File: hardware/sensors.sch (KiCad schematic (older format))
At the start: 16 parts

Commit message: Almost finished layout
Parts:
- removed L?: 330u, symbol L_Small
- C30, C31, C33: renamed from C?; footprint (none) -> Capacitors_SMD:C_1210
- C32: renamed from C?; value 47u -> 10u; footprint (none) -> Capacitors_ThroughHole:C_Radial_D5_L11_P2
- L3: renamed from L?; value Wurth 74275043 -> Wurth WE-CBF; footprint (none) -> Choke_SMD:Choke_SMD_1206_Standard
- P6: renamed from P?; value NORPS-12 -> NSL-19M51; footprint Luna_Optoelectronics_LDR:NORPS-12 -> TO_SOT_Packages_THT:TO-18_2Pin
- P7: renamed from P?; footprint Terminal_Blocks:TerminalBlock_Pheonix_MKDS1.5-5pol -> Connectors_Molex:Molex_KK-6410-05_05x2.54mm_Straight
- R24, R25, R26, R27, R28, R29, R30: renamed from R?; footprint (none) -> Resistors_SMD:R_1210
- gave numbers to parts that had none: 1
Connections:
- net 5VA: now also C32.1, C33.2, P7.3 (P3)
- net 3V3D: now reaches C31.1, L3.2, R25.1, R26.1, U3.2 (CSB), U3.6 (V_DDIO)
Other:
- note removed: "1.2kHz low pass"
- moved on the sheet: L3
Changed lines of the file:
@@
 LIBS:valves
 LIBS:wiznet
-LIBS:Sensors_STMicroelectronics
 LIBS:Sensors_Bosch
 LIBS:environment-sensor-cache
@@
 Enclosure must be aluminium to avoid hurting magnetic field measurements (mu << 1)\n\nhttps://physics.stackexchange.com/questions/6524/which-metals-can-cause-magnetic-interference-passively
 $Comp
-L Bosch_BME280 U?
+L Bosch_BME280 U3
 U 1 1 5893AF35
 P 7250 2400
-F 0 "U?" H 7250 2950 50  0000 C CNN
+F 0 "U3" H 7250 2950 50  0000 C CNN
 F 1 "Bosch_BME280" H 7250 1850 50  0000 C CNN
 F 2 "Bosch_Environment_Sensor:Bosch_BME280_LGA-8" H 7250 2400 60  0001 C CNN
@@
 $EndComp
 $Comp
-L C_Small C?
+L C_Small C31
 U 1 1 58F4F4F4
 P 5700 2400
-F 0 "C?" H 5750 2450 50  0000 L CNN
+F 0 "C31" H 5750 2450 50  0000 L CNN
 F 1 "100n" H 5750 2350 50  0000 L CNN
-F 2 "" H 5700 2400 50  0000 C CNN
+F 2 "Capacitors_SMD:C_1210" H 5700 2400 50  0001 C CNN
 F 3 "" H 5700 2400 50  0000 C CNN
 	1    5700 2400
@@
 Address = 1110110 (0x76)
 $Comp
-L R_Small R?
+L R_Small R26
 U 1 1 58F5028C
 P 6300 2450
-F 0 "R?" H 6350 2500 50  0000 L CNN
+F 0 "R26" H 6350 2500 50  0000 L CNN
 F 1 "4k7" H 6350 2400 50  0000 L CNN
-F 2 "" H 6300 2450 50  0000 C CNN
+F 2 "Resistors_SMD:R_1210" H 6300 2450 50  0001 C CNN
 F 3 "" H 6300 2450 50  0000 C CNN
 	1    6300 2450
@@
 $EndComp
 $Comp
-L R_Small R?
+L R_Small R25
 U 1 1 58F50586
 P 6200 2450
-F 0 "R?" H 6050 2500 50  0000 L CNN
+F 0 "R25" H 6050 2500 50  0000 L CNN
 F 1 "4k7" H 6000 2400 50  0000 L CNN
-F 2 "" H 6200 2450 50  0000 C CNN
+F 2 "Resistors_SMD:R_1210" H 6200 2450 50  0001 C CNN
 F 3 "" H 6200 2450 50  0000 C CNN
 	1    6200 2450
@@
 3V3A
 $Comp
-L C_Small C?
+L C_Small C30
 U 1 1 58F50E9D
 P 5300 2400
-F 0 "C?" H 5150 2450 50  0000 L CNN
+F 0 "C30" H 5150 2450 50  0000 L CNN
 F 1 "100n" H 5050 2350 50  0000 L CNN
-F 2 "" H 5300 2400 50  0000 C CNN
+F 2 "Capacitors_SMD:C_1210" H 5300 2400 50  0001 C CNN
 F 3 "" H 5300 2400 50  0000 C CNN
 	1    5300 2400
@@
 $EndComp
 $Comp
-L L_Small L?
+L L_Small L3
 U 1 1 58F5F3B6
-P 5500 2000
-F 0 "L?" H 5530 2040 50  0000 L CNN
-F 1 "Wurth 74275043" H 5530 1960 50  0000 L CNN
-F 2 "" H 5500 2000 50  0000 C CNN
-F 3 "" H 5500 2000 50  0000 C CNN
-	1    5500 2000
+P 5500 1400
+F 0 "L3" H 5530 1440 50  0000 L CNN
+F 1 "Wurth WE-CBF" H 5530 1360 50  0000 L CNN
+F 2 "Choke_SMD:Choke_SMD_1206_Standard" H 5500 1400 50  0001 C CNN
+F 3 "" H 5500 1400 50  0000 C CNN
+	1    5500 1400
 	0    -1   -1   0
 $EndComp
 $Comp
-L CONN_01X05 P?
+L CONN_01X05 P7
 U 1 1 58F69CD9
 P 7700 4725
-F 0 "P?" H 7700 5025 50  0000 C CNN
+F 0 "P7" H 7700 5025 50  0000 C CNN
 F 1 "PPD42" V 7800 4725 50  0000 C CNN
-F 2 "Terminal_Blocks:TerminalBlock_Pheonix_MKDS1.5-5pol" H 7700 4725 50  0001 C CNN
+F 2 "Connectors_Molex:Molex_KK-6410-05_05x2.54mm_Straight" H 7700 4725 50  0001 C CNN
 F 3 "" H 7700 4725 50  0000 C CNN
 	1    7700 4725
@@
 5VA
 $Comp
-L C_Small C?
+L C_Small C33
 U 1 1 58F4E0C6
 P 6625 4550
-F 0 "C?" H 6635 4620 50  0000 L CNN
+F 0 "C33" H 6635 4620 50  0000 L CNN
 F 1 "100n" H 6635 4470 50  0000 L CNN
-F 2 "" H 6625 4550 50  0000 C CNN
+F 2 "Capacitors_SMD:C_1210" H 6625 4550 50  0001 C CNN
 F 3 "" H 6625 4550 50  0000 C CNN
 	1    6625 4550
@@
 $EndComp
 Wire Wire Line
-	6200 2000 6200 2300
-Wire Wire Line
-	6200 2300 6200 2350
-Wire Wire Line
-	6200 2300 6300 2300
-Wire Wire Line
-	6300 2300 6650 2300
+	6200 2000 6200 2350
+Wire Wire Line
+	6200 2300 6650 2300
 Wire Wire Line
 	7850 2400 7925 2400
@@
 	5700 2800 5700 2500
 Wire Wire Line
-	5200 2800 5300 2800
-Wire Wire Line
-	5300 2800 5700 2800
-Wire Wire Line
-	5700 2800 6600 2800
-Wire Wire Line
-	6600 2800 6650 2800
+	5200 2800 6650 2800
 Wire Wire Line
 	6650 2700 6600 2700
@@
 	6500 2400 6500 2600
 Wire Wire Line
-	6500 2600 6300 2600
-Wire Wire Line
-	6300 2600 6150 2600
+	6500 2600 6150 2600
 Wire Wire Line
 	6300 2600 6300 2550
@@
 	6550 2500 6550 2700
 Wire Wire Line
-	6550 2700 6200 2700
-Wire Wire Line
-	6200 2700 6150 2700
+	6550 2700 6150 2700
 Wire Wire Line
 	6200 2700 6200 2550
@@
 Connection ~ 6200 2700
 Wire Wire Line
-	5200 2100 5300 2100
-Wire Wire Line
-	5300 2100 6650 2100
+	5200 2100 6650 2100
 Wire Wire Line
 	5300 2800 5300 2500
 Connection ~ 5700 2800
-Wire Wire Line
-	5300 2000 5300 2100
-Wire Wire Line
-	5300 2100 5300 2300
 Connection ~ 5300 2100
 Wire Wire Line
-	5600 2000 5700 2000
-Wire Wire Line
-	5700 2000 6200 2000
-Wire Wire Line
-	6200 2000 6650 2000
-Wire Wire Line
-	5400 2000 5300 2000
+	5600 2000 6650 2000
 Connection ~ 5300 2800
 $Comp
-L CP_Small C?
+L CP_Small C32
 U 1 1 58F4E384
 P 6475 4550
-F 0 "C?" H 6485 4620 50  0000 L CNN
-F 1 "47u" H 6485 4470 50  0000 L CNN
-F 2 "" H 6475 4550 50  0000 C CNN
+F 0 "C32" H 6485 4620 50  0000 L CNN
+F 1 "10u" H 6485 4470 50  0000 L CNN
+F 2 "Capacitors_ThroughHole:C_Radial_D5_L11_P2" H 6475 4550 50  0001 C CNN
 F 3 "" H 6475 4550 50  0000 C CNN
 	1    6475 4550
@@
 $EndComp
 Wire Wire Line
-	6025 4375 6475 4375
-Wire Wire Line
-	6475 4375 6625 4375
-Wire Wire Line
-	6625 4375 7350 4375
+	6025 4375 7350 4375
 Wire Wire Line
 	6475 4375 6475 4450
@@
 Connection ~ 6625 4375
 Wire Wire Line
-	6300 4725 6475 4725
-Wire Wire Line
-	6475 4725 6625 4725
-Wire Wire Line
-	6625 4725 7500 4725
+	6025 4725 7500 4725
 Wire Wire Line
 	6475 4725 6475 4650
@@
 Tempertature/humidity/pressure sensor
 $Comp
-L R_Small R?
+L R_Small R29
 U 1 1 58F597C3
 P 6850 5100
-F 0 "R?" H 6700 5100 50  0000 L CNN
+F 0 "R29" H 6700 5100 50  0000 L CNN
 F 1 "10k" H 6675 5175 50  0000 L CNN
-F 2 "" H 6850 5100 50  0000 C CNN
+F 2 "Resistors_SMD:R_1210" H 6850 5100 50  0001 C CNN
 F 3 "" H 6850 5100 50  0000 C CNN
 	1    6850 5100
@@
 $EndComp
 $Comp
-L R_Small R?
+L R_Small R27
 U 1 1 58F5987E
 P 6675 5100
-F 0 "R?" H 6725 5100 50  0000 L CNN
+F 0 "R27" H 6725 5100 50  0000 L CNN
 F 1 "10k" H 6725 5175 50  0000 L CNN
-F 2 "" H 6675 5100 50  0000 C CNN
+F 2 "Resistors_SMD:R_1210" H 6675 5100 50  0001 C CNN
 F 3 "" H 6675 5100 50  0000 C CNN
 	1    6675 5100
@@
 $EndComp
 $Comp
-L R_Small R?
+L R_Small R30
 U 1 1 58F59C27
 P 6850 5400
-F 0 "R?" H 6700 5400 50  0000 L CNN
+F 0 "R30" H 6700 5400 50  0000 L CNN
 F 1 "10k" H 6675 5475 50  0000 L CNN
-F 2 "" H 6850 5400 50  0000 C CNN
+F 2 "Resistors_SMD:R_1210" H 6850 5400 50  0001 C CNN
 F 3 "" H 6850 5400 50  0000 C CNN
 	1    6850 5400
@@
 $EndComp
 $Comp
-L R_Small R?
+L R_Small R28
 U 1 1 58F59C75
 P 6675 5400
-F 0 "R?" H 6725 5400 50  0000 L CNN
+F 0 "R28" H 6725 5400 50  0000 L CNN
 F 1 "10k" H 6725 5475 50  0000 L CNN
-F 2 "" H 6675 5400 50  0000 C CNN
+F 2 "Resistors_SMD:R_1210" H 6675 5400 50  0001 C CNN
 F 3 "" H 6675 5400 50  0000 C CNN
 	1    6675 5400
@@
 	6600 5250 6675 5250
 Wire Wire Line
-	6675 5200 6675 5250
-Wire Wire Line
-	6675 5250 6675 5300
+	6675 5200 6675 5300
 Connection ~ 6675 5250
 Wire Wire Line
@@
 	6850 5000 6850 4625
 Wire Wire Line
-	6850 5200 6850 5250
-Wire Wire Line
-	6850 5250 6850 5300
+	6850 5200 6850 5300
 Wire Wire Line
 	6925 5250 6850 5250
@@
 GND
 Wire Wire Line
-	6600 5575 6675 5575
-Wire Wire Line
-	6675 5575 6850 5575
+	6600 5575 6850 5575
 Wire Wire Line
 	6675 5575 6675 5500
@@
 Connection ~ 6675 5575
 $Comp
-L L_Small L?
-U 1 1 58F5B341
-P 6200 4725
-F 0 "L?" H 6230 4765 50  0000 L CNN
-F 1 "330u" H 6230 4685 50  0000 L CNN
-F 2 "" H 6200 4725 50  0000 C CNN
-F 3 "" H 6200 4725 50  0000 C CNN
-	1    6200 4725
-	0    -1   -1   0
-$EndComp
-Wire Wire Line
-	6025 4725 6100 4725
-Text Notes 6075 4325 0    60   ~ 0
-1.2kHz low pass
-$Comp
-L CONN_01X02 P?
+L CONN_01X02 P6
 U 1 1 58F66D18
 P 4200 4475
-F 0 "P?" H 4200 4625 50  0000 C CNN
-F 1 "NORPS-12" V 4300 4475 50  0000 C CNN
-F 2 "Luna_Optoelectronics_LDR:NORPS-12" H 4200 4475 50  0001 C CNN
+F 0 "P6" H 4200 4625 50  0000 C CNN
+F 1 "NSL-19M51" V 4300 4475 50  0000 C CNN
+F 2 "TO_SOT_Packages_THT:TO-18_2Pin" H 4200 4475 50  0001 C CNN
 F 3 "" H 4200 4475 50  0000 C CNN
 	1    4200 4475
@@
 LDR_OUT
 Wire Wire Line
-	4000 4525 3825 4525
-Wire Wire Line
-	3825 4525 3750 4525
-$Comp
-L R_Small R?
+	3750 4525 4000 4525
+$Comp
+L R_Small R24
 U 1 1 58F672FB
 P 3825 4700
-F 0 "R?" H 3855 4720 50  0000 L CNN
+F 0 "R24" H 3855 4720 50  0000 L CNN
 F 1 "10k" H 3855 4660 50  0000 L CNN
-F 2 "" H 3825 4700 50  0000 C CNN
+F 2 "Resistors_SMD:R_1210" H 3825 4700 50  0001 C CNN
 F 3 "" H 3825 4700 50  0000 C CNN
 	1    3825 4700
@@
 Text Notes 3650 4200 0    60   ~ 0
 Light sensor
+Text Label 5775 1400 0    60   ~ 0
+3V3D
+Wire Wire Line
+	5775 1400 5600 1400
+Text HLabel 5200 1400 0    60   Input ~ 0
+3V3A
+Wire Wire Line
+	5200 1400 5400 1400
+Wire Wire Line
+	5300 2300 5300 2100
+Text Label 5600 2000 2    60   ~ 0
+3V3D
 $EndSCHEMATC

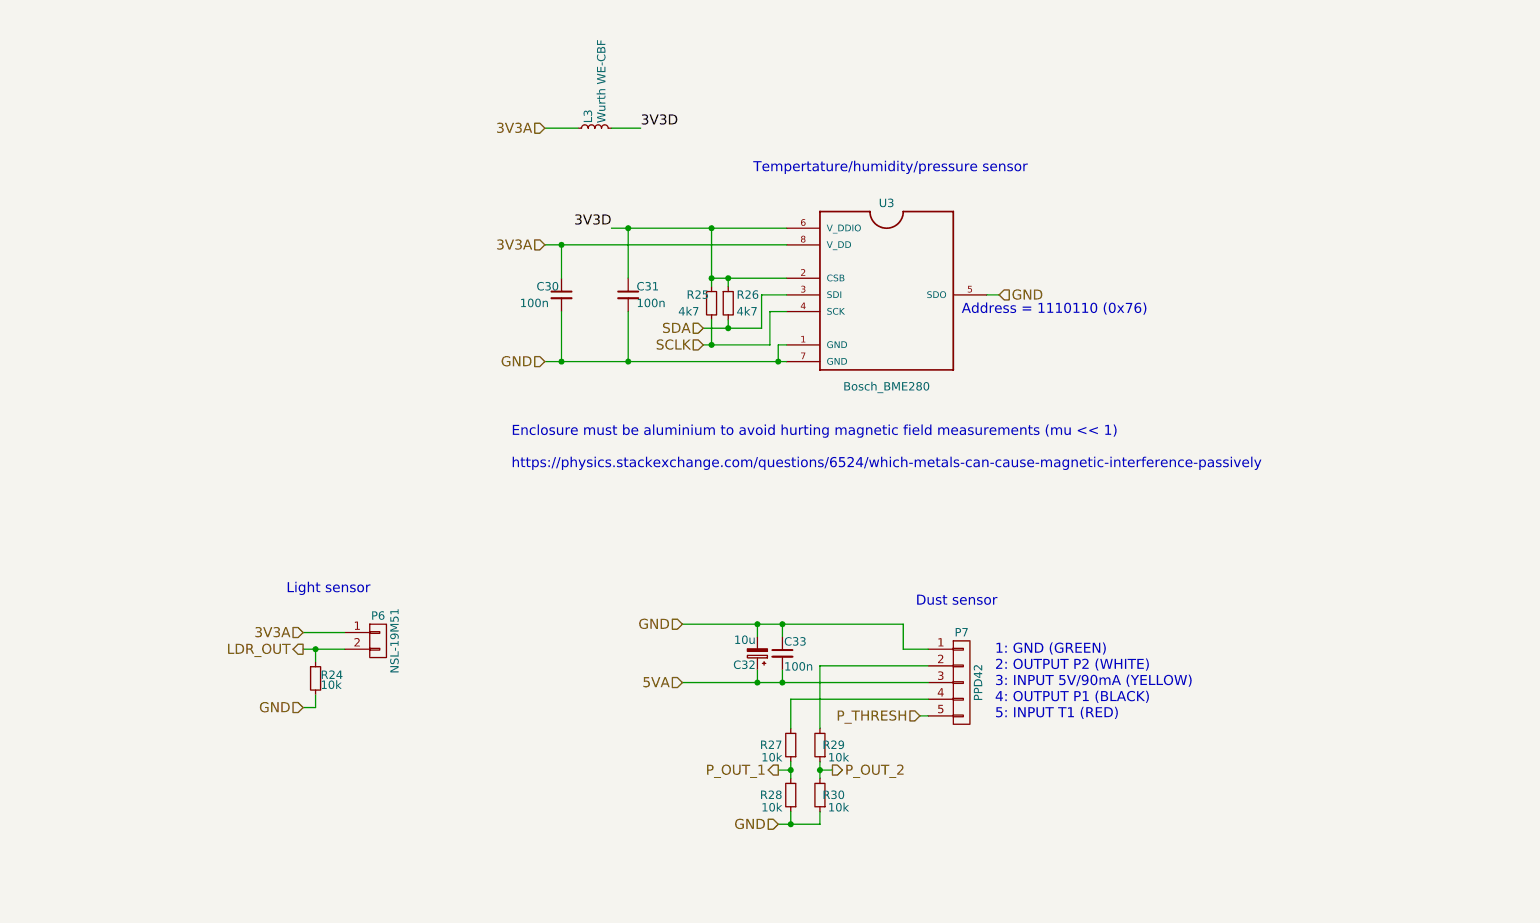
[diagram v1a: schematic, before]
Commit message: Revision of board to address issues
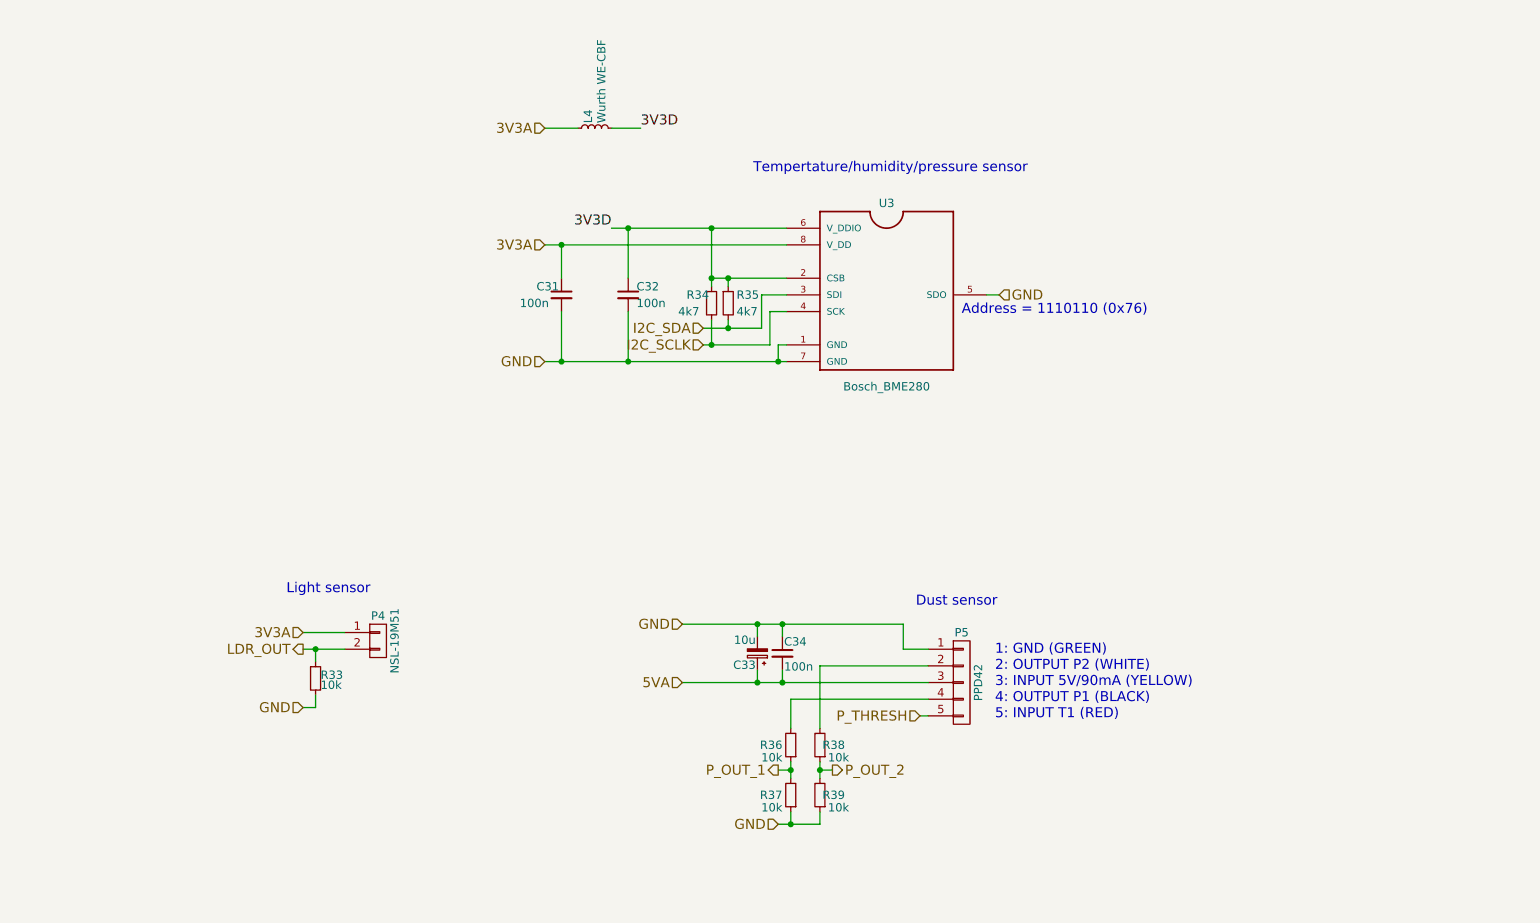
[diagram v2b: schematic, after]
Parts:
- C31: renamed from C30; footprint Capacitors_SMD:C_1210 -> Capacitors_SMD:C_1206
- C32: renamed from C31; footprint Capacitors_SMD:C_1210 -> Capacitors_SMD:C_1206
- C34: renamed from C33; footprint Capacitors_SMD:C_1210 -> Capacitors_SMD:C_1206
- R33: renamed from R24; footprint Resistors_SMD:R_1210 -> Resistors_SMD:R_1206
- R34: renamed from R25; footprint Resistors_SMD:R_1210 -> Resistors_SMD:R_1206
- R35: renamed from R26; footprint Resistors_SMD:R_1210 -> Resistors_SMD:R_1206
- R36: renamed from R27; footprint Resistors_SMD:R_1210 -> Resistors_SMD:R_1206
- R37: renamed from R28; footprint Resistors_SMD:R_1210 -> Resistors_SMD:R_1206
- R38: renamed from R29; footprint Resistors_SMD:R_1210 -> Resistors_SMD:R_1206
- R39: renamed from R30; footprint Resistors_SMD:R_1210 -> Resistors_SMD:R_1206
- renumbered C32 to C33, L3 to L4, P6 to P4, P7 to P5
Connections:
- net SCLK renamed I2C_SCLK
- net SDA renamed I2C_SDA
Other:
- note removed: "Enclosure must be aluminium to avoid hurting magnetic field measurements (mu << 1)\n\nhttps://physics.stackexchange.com/questions/6524/which-metals-can-cause-magnetic-interference-passively"
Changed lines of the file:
@@
 LIBS:wiznet
 LIBS:Sensors_Bosch
+LIBS:cetus
 LIBS:environment-sensor-cache
 EELAYER 25 0
@@
 Text HLabel 7925 2400 2    60   Input ~ 0
 GND
-Text Notes 5000 3450 0    60   ~ 0
-Enclosure must be aluminium to avoid hurting magnetic field measurements (mu << 1)\n\nhttps://physics.stackexchange.com/questions/6524/which-metals-can-cause-magnetic-interference-passively
 $Comp
 L Bosch_BME280 U3
@@
 $EndComp
 $Comp
-L C_Small C31
+L C_Small C32
 U 1 1 58F4F4F4
 P 5700 2400
-F 0 "C31" H 5750 2450 50  0000 L CNN
+F 0 "C32" H 5750 2450 50  0000 L CNN
 F 1 "100n" H 5750 2350 50  0000 L CNN
-F 2 "Capacitors_SMD:C_1210" H 5700 2400 50  0001 C CNN
+F 2 "Capacitors_SMD:C_1206" H 5700 2400 50  0001 C CNN
 F 3 "" H 5700 2400 50  0000 C CNN
 	1    5700 2400
@@
 $EndComp
 Text HLabel 6150 2700 0    60   Input ~ 0
-SCLK
+I2C_SCLK
 Text HLabel 6150 2600 0    60   Input ~ 0
-SDA
+I2C_SDA
 Text Notes 7700 2525 0    60   ~ 0
 Address = 1110110 (0x76)
 $Comp
-L R_Small R26
+L R_Small R35
 U 1 1 58F5028C
 P 6300 2450
-F 0 "R26" H 6350 2500 50  0000 L CNN
+F 0 "R35" H 6350 2500 50  0000 L CNN
 F 1 "4k7" H 6350 2400 50  0000 L CNN
-F 2 "Resistors_SMD:R_1210" H 6300 2450 50  0001 C CNN
+F 2 "Resistors_SMD:R_1206" H 6300 2450 50  0001 C CNN
 F 3 "" H 6300 2450 50  0000 C CNN
 	1    6300 2450
@@
 $EndComp
 $Comp
-L R_Small R25
+L R_Small R34
 U 1 1 58F50586
 P 6200 2450
-F 0 "R25" H 6050 2500 50  0000 L CNN
+F 0 "R34" H 6050 2500 50  0000 L CNN
 F 1 "4k7" H 6000 2400 50  0000 L CNN
-F 2 "Resistors_SMD:R_1210" H 6200 2450 50  0001 C CNN
+F 2 "Resistors_SMD:R_1206" H 6200 2450 50  0001 C CNN
 F 3 "" H 6200 2450 50  0000 C CNN
 	1    6200 2450
@@
 3V3A
 $Comp
-L C_Small C30
+L C_Small C31
 U 1 1 58F50E9D
 P 5300 2400
-F 0 "C30" H 5150 2450 50  0000 L CNN
+F 0 "C31" H 5150 2450 50  0000 L CNN
 F 1 "100n" H 5050 2350 50  0000 L CNN
-F 2 "Capacitors_SMD:C_1210" H 5300 2400 50  0001 C CNN
+F 2 "Capacitors_SMD:C_1206" H 5300 2400 50  0001 C CNN
 F 3 "" H 5300 2400 50  0000 C CNN
 	1    5300 2400
@@
 $EndComp
 $Comp
-L L_Small L3
+L L_Small L4
 U 1 1 58F5F3B6
 P 5500 1400
-F 0 "L3" H 5530 1440 50  0000 L CNN
+F 0 "L4" H 5530 1440 50  0000 L CNN
 F 1 "Wurth WE-CBF" H 5530 1360 50  0000 L CNN
 F 2 "Choke_SMD:Choke_SMD_1206_Standard" H 5500 1400 50  0001 C CNN
@@
 $EndComp
 $Comp
-L CONN_01X05 P7
+L CONN_01X05 P5
 U 1 1 58F69CD9
 P 7700 4725
-F 0 "P7" H 7700 5025 50  0000 C CNN
+F 0 "P5" H 7700 5025 50  0000 C CNN
 F 1 "PPD42" V 7800 4725 50  0000 C CNN
 F 2 "Connectors_Molex:Molex_KK-6410-05_05x2.54mm_Straight" H 7700 4725 50  0001 C CNN
@@
 5VA
 $Comp
-L C_Small C33
+L C_Small C34
 U 1 1 58F4E0C6
 P 6625 4550
-F 0 "C33" H 6635 4620 50  0000 L CNN
+F 0 "C34" H 6635 4620 50  0000 L CNN
 F 1 "100n" H 6635 4470 50  0000 L CNN
-F 2 "Capacitors_SMD:C_1210" H 6625 4550 50  0001 C CNN
+F 2 "Capacitors_SMD:C_1206" H 6625 4550 50  0001 C CNN
 F 3 "" H 6625 4550 50  0000 C CNN
 	1    6625 4550
@@
 Connection ~ 5300 2800
 $Comp
-L CP_Small C32
+L CP_Small C33
 U 1 1 58F4E384
 P 6475 4550
-F 0 "C32" H 6485 4620 50  0000 L CNN
+F 0 "C33" H 6485 4620 50  0000 L CNN
 F 1 "10u" H 6485 4470 50  0000 L CNN
 F 2 "Capacitors_ThroughHole:C_Radial_D5_L11_P2" H 6475 4550 50  0001 C CNN
@@
 Tempertature/humidity/pressure sensor
 $Comp
-L R_Small R29
+L R_Small R38
 U 1 1 58F597C3
 P 6850 5100
-F 0 "R29" H 6700 5100 50  0000 L CNN
+F 0 "R38" H 6700 5100 50  0000 L CNN
 F 1 "10k" H 6675 5175 50  0000 L CNN
-F 2 "Resistors_SMD:R_1210" H 6850 5100 50  0001 C CNN
+F 2 "Resistors_SMD:R_1206" H 6850 5100 50  0001 C CNN
 F 3 "" H 6850 5100 50  0000 C CNN
 	1    6850 5100
@@
 $EndComp
 $Comp
-L R_Small R27
+L R_Small R36
 U 1 1 58F5987E
 P 6675 5100
-F 0 "R27" H 6725 5100 50  0000 L CNN
+F 0 "R36" H 6725 5100 50  0000 L CNN
 F 1 "10k" H 6725 5175 50  0000 L CNN
-F 2 "Resistors_SMD:R_1210" H 6675 5100 50  0001 C CNN
+F 2 "Resistors_SMD:R_1206" H 6675 5100 50  0001 C CNN
 F 3 "" H 6675 5100 50  0000 C CNN
 	1    6675 5100
@@
 $EndComp
 $Comp
-L R_Small R30
+L R_Small R39
 U 1 1 58F59C27
 P 6850 5400
-F 0 "R30" H 6700 5400 50  0000 L CNN
+F 0 "R39" H 6700 5400 50  0000 L CNN
 F 1 "10k" H 6675 5475 50  0000 L CNN
-F 2 "Resistors_SMD:R_1210" H 6850 5400 50  0001 C CNN
+F 2 "Resistors_SMD:R_1206" H 6850 5400 50  0001 C CNN
 F 3 "" H 6850 5400 50  0000 C CNN
 	1    6850 5400
@@
 $EndComp
 $Comp
-L R_Small R28
+L R_Small R37
 U 1 1 58F59C75
 P 6675 5400
-F 0 "R28" H 6725 5400 50  0000 L CNN
+F 0 "R37" H 6725 5400 50  0000 L CNN
 F 1 "10k" H 6725 5475 50  0000 L CNN
-F 2 "Resistors_SMD:R_1210" H 6675 5400 50  0001 C CNN
+F 2 "Resistors_SMD:R_1206" H 6675 5400 50  0001 C CNN
 F 3 "" H 6675 5400 50  0000 C CNN
 	1    6675 5400
@@
 Connection ~ 6675 5575
 $Comp
-L CONN_01X02 P6
+L CONN_01X02 P4
 U 1 1 58F66D18
 P 4200 4475
-F 0 "P6" H 4200 4625 50  0000 C CNN
+F 0 "P4" H 4200 4625 50  0000 C CNN
 F 1 "NSL-19M51" V 4300 4475 50  0000 C CNN
 F 2 "TO_SOT_Packages_THT:TO-18_2Pin" H 4200 4475 50  0001 C CNN
@@
 	3750 4525 4000 4525
 $Comp
-L R_Small R24
+L R_Small R33
 U 1 1 58F672FB
 P 3825 4700
-F 0 "R24" H 3855 4720 50  0000 L CNN
+F 0 "R33" H 3855 4720 50  0000 L CNN
 F 1 "10k" H 3855 4660 50  0000 L CNN
-F 2 "Resistors_SMD:R_1210" H 3825 4700 50  0001 C CNN
+F 2 "Resistors_SMD:R_1206" H 3825 4700 50  0001 C CNN
 F 3 "" H 3825 4700 50  0000 C CNN
 	1    3825 4700

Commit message: New revision to board
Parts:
- removed P4: NSL-19M51, TO_SOT_Packages_THT:TO-18_2Pin, symbol CONN_01X02
- added P8: DS18B20, Connectors_Molex:Molex_KK-6410-03_03x2.54mm_Straight, symbol CONN_01X03
- added R38: 4k7, Resistors_SMD:R_1206, symbol R_Small
- added R39: NSL-19M51, LDRs_NSL:NSL_19M51, symbol NSL-19M51
- U5: renamed from U3; footprint Bosch_Environment_Sensor:Bosch_BME280_LGA-8 -> Sensors_LGA:Bosch_BME280_LGA-8
- renumbered C31 to C36, C32 to C37, C33 to C38, C34 to C39, L4 to L5, P5 to P9, R34 to R32, R35 to R33, R36 to R34, R37 to R35, R38 to R36, R39 to R37, R33 to R40
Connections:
- net 3V3A: now also R39.2
- net 3V3D: now also P8.1 (P1), R38.2
- net GND: now also P8.3 (P3)
- net LDR_OUT renamed LDR
- net LDR: now also R39.1
- net P_OUT_1 renamed DUST_1
- net P_OUT_2 renamed DUST_2
- net P_THRESH renamed DUST_2_THRESH
- new net DS18B20: P8.2 (P2), R38.1
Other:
- note added: "Temperature sensor"
- moved on the sheet: C36, C37, C38, C39, L5, P9, R32, R33, R34, R35, R36, R37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
